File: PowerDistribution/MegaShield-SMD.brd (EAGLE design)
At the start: 109.2 x 53.3 mm, 37 parts, among them IC1 TLE5206-2G, IC2 TLE5206-2G, IC3 TLE5206-2G, J10 DCJ0202

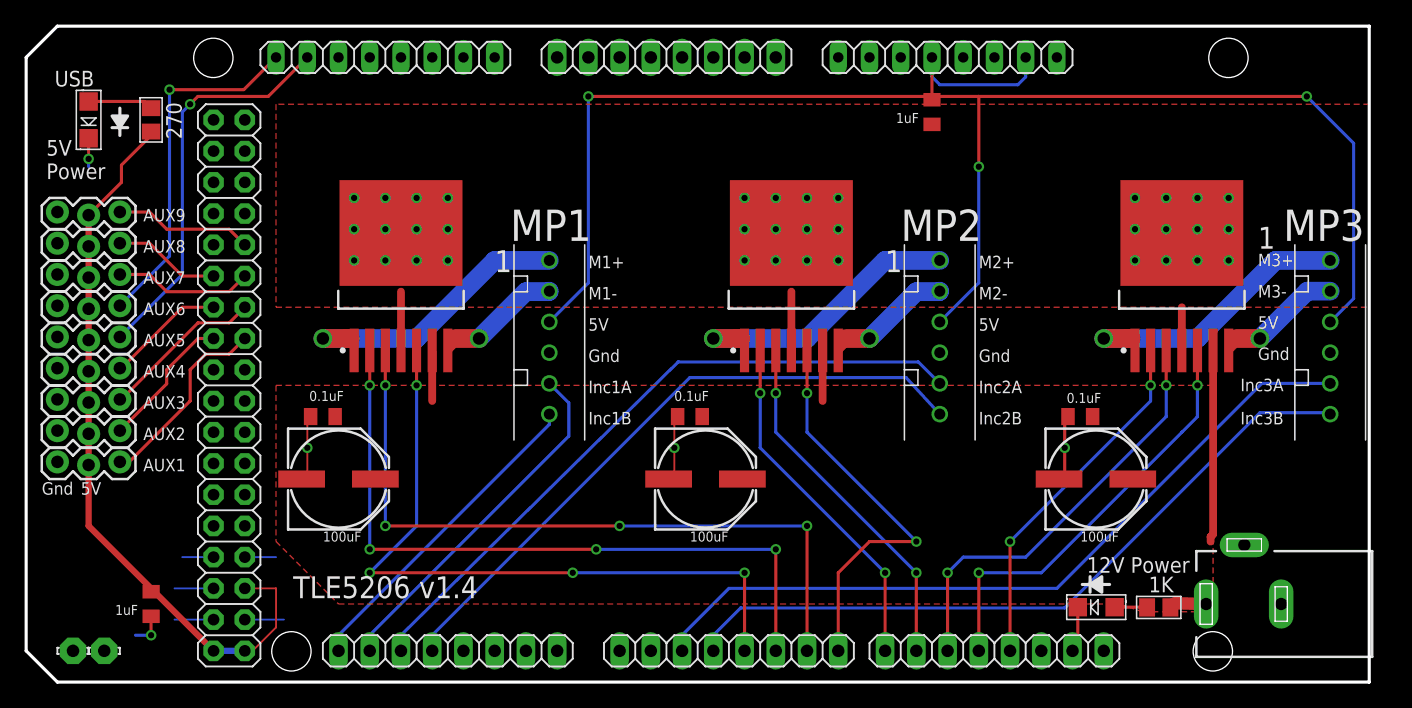
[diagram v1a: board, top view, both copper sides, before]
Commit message: Move Motor Connectors up to avoid Arduino USB connector on MP3
... but keep them in line, 'because'.
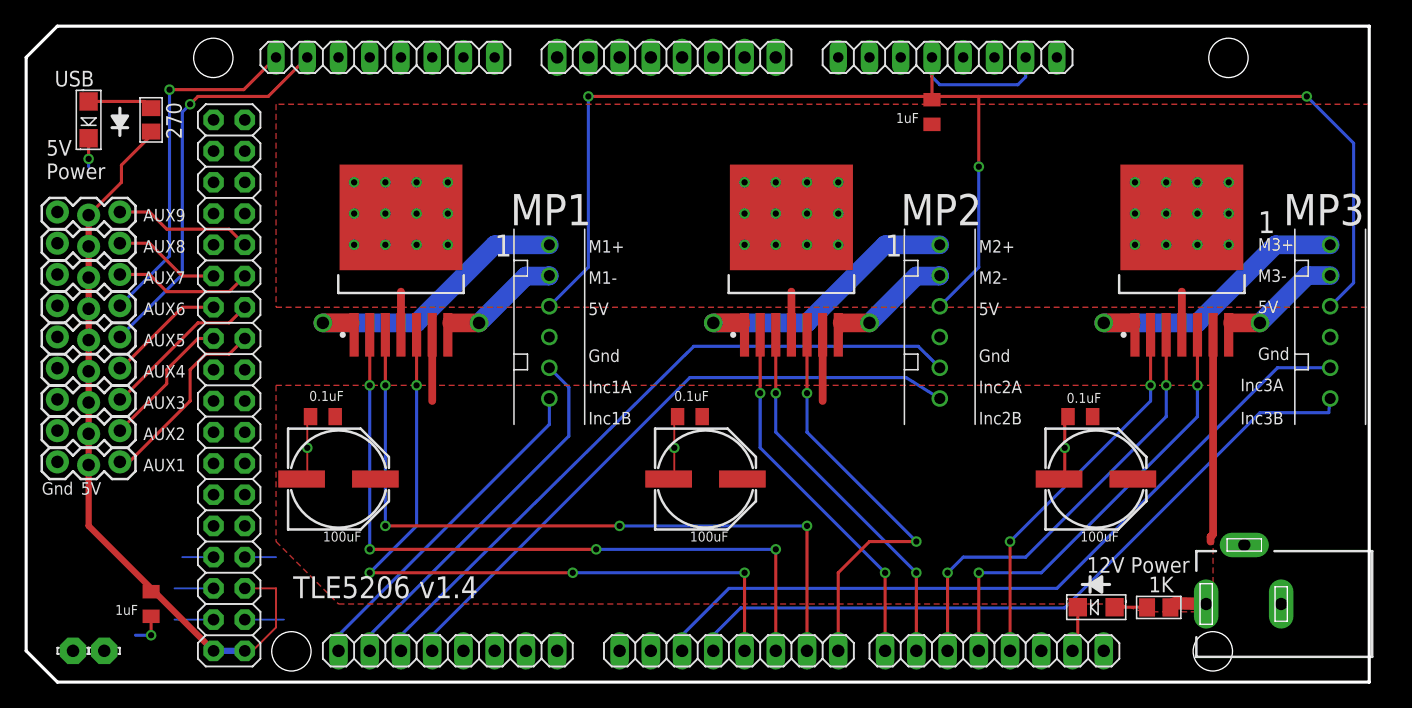
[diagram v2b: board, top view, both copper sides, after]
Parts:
- moved MP1 1.27 mm to (42.5, 35.6)
- moved MP2 1.27 mm to (74.3, 35.6)
- moved MP3 1.27 mm to (106.0, 35.6)
- moved IC1 1.27 mm to (30.5, 34.3)
- moved IC2 1.27 mm to (62.2, 34.3)
- moved IC3 1.27 mm to (94.0, 34.3)
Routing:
- net 5V: track 193.9 -> 190.0 mm
- net 12V: track 26.9 -> 30.7 mm
- net GND: track 53.6 -> 51.1 mm
- net ENA: track 57.4 -> 58.7 mm
- net IN6: track 34.8 -> 36.0 mm
- net IN4: track 33.0 -> 34.2 mm
- net IN2: track 56.5 -> 57.8 mm
- net INC1B: track 26.4 -> 27.6 mm
- net INC1A: track 29.1 -> 30.4 mm
- net IN3: track 29.2 -> 30.4 mm
- net ENC: track 29.2 -> 30.4 mm
- net ENB: track 28.6 -> 29.9 mm
- net IN5: track 34.8 -> 36.0 mm
- net IN1: track 58.7 -> 60.0 mm
- net INC3B: track 59.0 -> 60.0 mm
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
